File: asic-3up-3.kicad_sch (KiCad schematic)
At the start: 73 parts, among them J10 Conn_01x01, J11 Conn_01x01, J21 Conn_01x01, U4 SN74AVC4T774, U5 25MHz, U66 MCP1824T-1202E/OT, U67 MCP1824T-1202E/OT, U68 MCP1824T-1202E/OT, U69 MCP1824T-0802E, U70 MCP1824T-0802E, U71 MCP1824T-0802E, U72 BM1362AC_MODE1, U73 BM1362AC_MODE0, U74 BM1362AC_MODE1

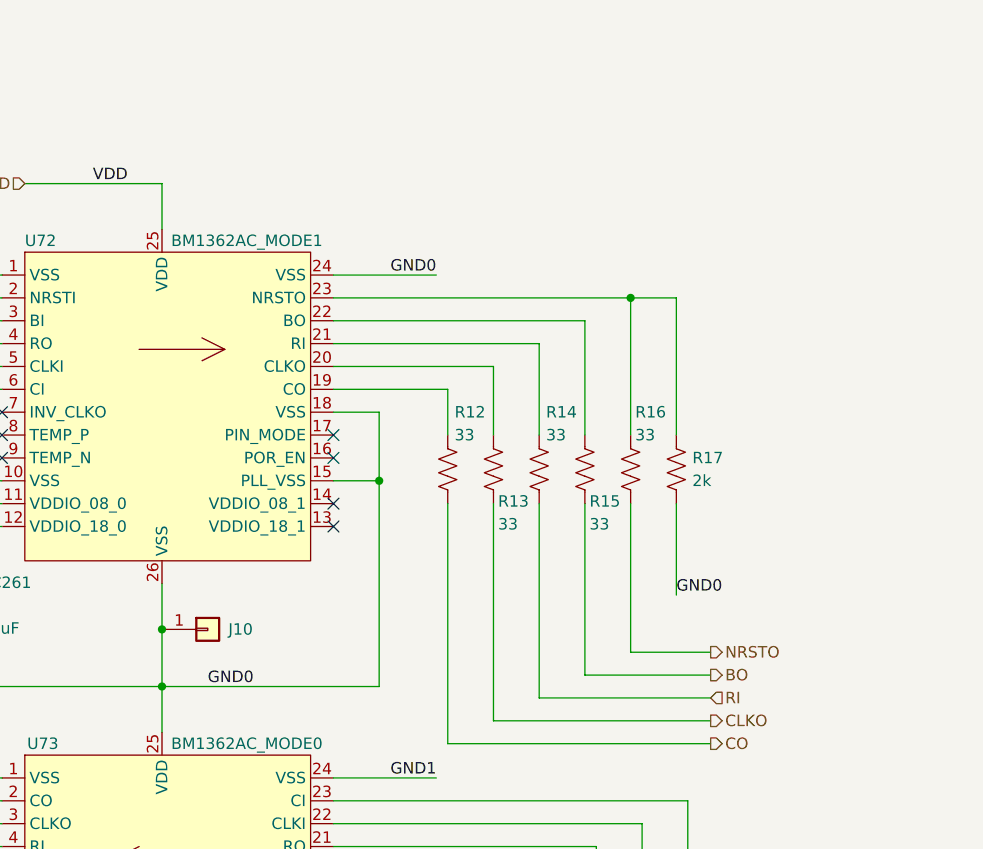
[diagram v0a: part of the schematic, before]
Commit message: added RI pullup resistors for #16. updated BOM. bumped version number to 3
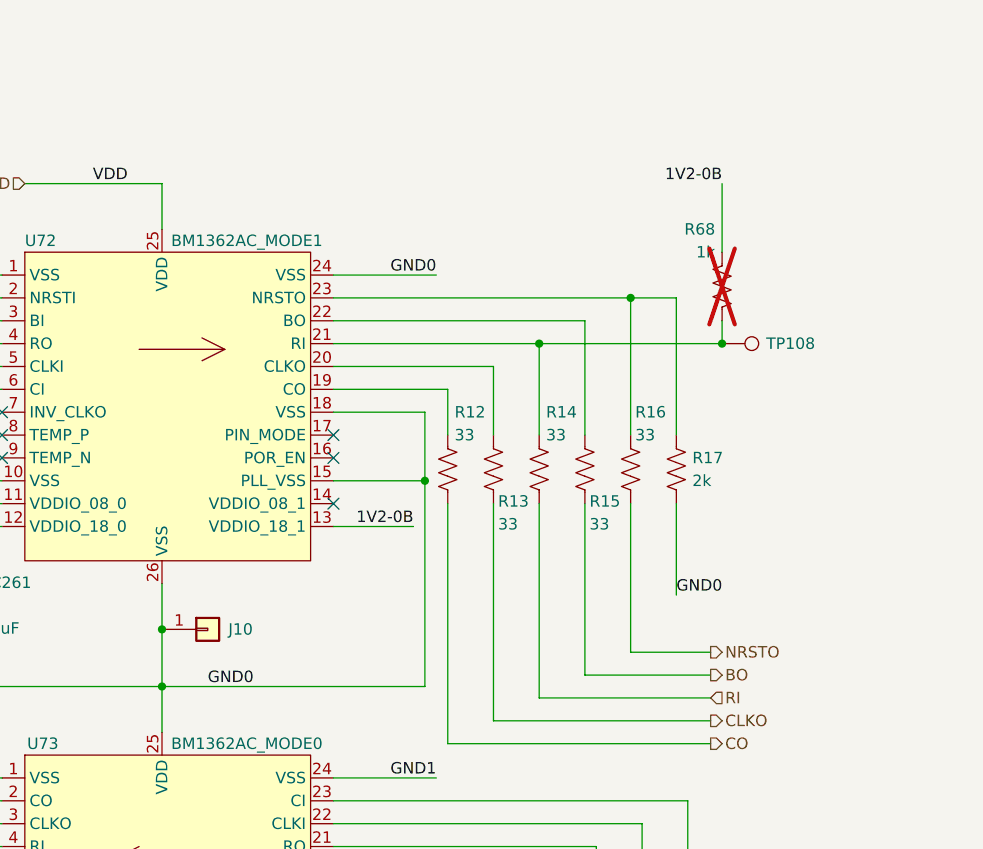
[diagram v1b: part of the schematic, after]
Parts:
- added R68: 1k, Resistor_SMD:R_0402_1005Metric, symbol Device:R_US
- added TP108: TestPoint, TestPoint:TestPoint_Pad_D1.0mm, symbol Connector:TestPoint
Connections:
- net 1V2-0B: now reaches U72.13 (VDDIO_18_1)
- net 1V2-0B: now also R68.1
- net at R14.1, U72.21 (RI): now also R68.2, TP108.1
- no-connect marks 27 -> 26
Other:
- title: (none) -> emberOne/00
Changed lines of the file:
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@@
 	(paper "A3")
 	(title_block
-		(date "2024-11-25")
-		(rev "2")
+		(title "emberOne/00")
+		(date "2025-02-25")
+		(rev "3")
 	)
 	(text "Reference Voltage Regulators"
@@
 	)
 	(junction
+		(at 311.15 105.41)
+		(diameter 0)
+		(color 0 0 0 0)
+	)
+	(junction
 		(at 73.66 64.77)
 		(diameter 0)
@@
 	)
 	(junction
-		(at 273.05 120.65)
-		(diameter 0)
-		(color 0 0 0 0)
-	)
-	(junction
 		(at 220.98 199.39)
 		(diameter 0)
@@
 	)
 	(junction
+		(at 278.13 120.65)
+		(diameter 0)
+		(color 0 0 0 0)
+	)
+	(junction
 		(at 356.87 222.25)
 		(diameter 0)
@@
 	)
 	(junction
+		(at 290.83 105.41)
+		(diameter 0)
+		(color 0 0 0 0)
+	)
+	(junction
 		(at 91.44 163.83)
 		(diameter 0.9144)
@@
 	)
 	(no_connect
-		(at 267.97 125.73)
-	)
-	(no_connect
 		(at 231.14 224.79)
 	)
@@
 	(wire
 		(pts
-			(xy 273.05 113.03) (xy 267.97 113.03)
+			(xy 278.13 113.03) (xy 267.97 113.03)
 		)
 		(stroke
@@
 	(wire
 		(pts
-			(xy 273.05 143.51) (xy 273.05 120.65)
+			(xy 278.13 143.51) (xy 278.13 120.65)
 		)
 		(stroke
@@
 	(wire
 		(pts
-			(xy 248.92 143.51) (xy 273.05 143.51)
+			(xy 248.92 143.51) (xy 278.13 143.51)
 		)
 		(stroke
@@
 	(wire
 		(pts
+			(xy 311.15 87.63) (xy 311.15 95.25)
+		)
+		(stroke
+			(width 0)
+			(type default)
+		)
+	)
+	(wire
+		(pts
 			(xy 207.01 219.71) (xy 207.01 214.63)
 		)
@@
 	(wire
 		(pts
+			(xy 290.83 105.41) (xy 311.15 105.41)
+		)
+		(stroke
+			(width 0)
+			(type default)
+		)
+	)
+	(wire
+		(pts
 			(xy 87.63 166.37) (xy 86.36 166.37)
 		)
@@
 	(wire
 		(pts
-			(xy 267.97 120.65) (xy 273.05 120.65)
+			(xy 267.97 120.65) (xy 278.13 120.65)
 		)
 		(stroke
@@
 	(wire
 		(pts
+			(xy 311.15 105.41) (xy 311.15 102.87)
+		)
+		(stroke
+			(width 0)
+			(type default)
+		)
+	)
+	(wire
+		(pts
 			(xy 152.4 231.14) (xy 152.4 234.95)
 		)
@@
 	(wire
 		(pts
-			(xy 273.05 120.65) (xy 273.05 113.03)
+			(xy 278.13 120.65) (xy 278.13 113.03)
 		)
 		(stroke
@@
 	(wire
 		(pts
+			(xy 267.97 125.73) (xy 276.86 125.73)
+		)
+		(stroke
+			(width 0)
+			(type default)
+		)
+	)
+	(wire
+		(pts
 			(xy 312.42 179.07) (xy 312.42 186.69)
 		)
@@
 		)
 	)
+	(label "1V2-0B"
+		(at 311.15 87.63 180)
+		(effects
+			(font
+				(size 1.27 1.27)
+			)
+			(justify right bottom)
+		)
+	)
 	(label "3V3"
 		(at 106.68 34.29 0)
@@
 		)
 	)
+	(label "1V2-0B"
+		(at 276.86 125.73 180)
+		(effects
+			(font
+				(size 1.27 1.27)
+			)
+			(justify right bottom)
+		)
+	)
 	(label "GND2"
 		(at 105.41 52.07 0)
@@
 	)
 	(symbol
+		(lib_id "Device:R_US")
+		(at 311.15 99.06 0)
+		(mirror y)
+		(unit 1)
+		(exclude_from_sim no)
+		(in_bom yes)
+		(on_board yes)
+		(dnp yes)
+		(property "Reference" "R68"
+			(at 310.388 92.71 0)
+			(effects
+				(font
+					(size 1.27 1.27)
+				)
+				(justify left)
+			)
+		)
+		(property "Value" "1k"
+			(at 310.388 95.25 0)
+			(effects
+				(font
+					(size 1.27 1.27)
+				)
+				(justify left)
+			)
+		)
+		(property "Footprint" "Resistor_SMD:R_0402_1005Metric"
+			(at 310.134 99.314 90)
+			(effects
+				(font
+					(size 1.27 1.27)
+				)
+				(hide yes)
+			)
+		)
+		(property "Datasheet" "~"
+			(at 311.15 99.06 0)
+			(effects
+				(font
+					(size 1.27 1.27)
+				)
+				(hide yes)
+			)
+		)
+		(property "Description" "Resistor, US symbol"
+			(at 311.15 99.06 0)
+			(effects
+				(font
+					(size 1.27 1.27)
+				)
+				(hide yes)
+			)
+		)
+		(property "DK" ""
+			(at 311.15 99.06 0)
+			(effects
+				(font
+					(size 1.27 1.27)
+				)
+				(hide yes)
+			)
+		)
+		(property "PARTNO" ""
+			(at 311.15 99.06 0)
+			(effects
+				(font
+					(size 1.27 1.27)
+				)
+				(hide yes)
+			)
+		)
+		(pin "1"
+		)
+		(pin "2"
+		)
+		(instances
+			(project "emberone"
+				(path "/b036224c-4cdf-48cc-81df-19bc5283ebd2/75fd7cab-4b1e-4fa4-8631-02e52962bbf8"
+					(reference "R68")
+					(unit 1)
+				)
+			)
+		)
+	)
+	(symbol
 		(lib_id "bitaxe:MCP1824")
 		(at 76.2 222.25 0)
@@
 					(unit 1)
 				)
+			)
+		)
+	)
+	(symbol
+		(lib_id "Connector:TestPoint")
+		(at 311.15 105.41 270)
+		(unit 1)
+		(exclude_from_sim no)
+		(in_bom no)
+		(on_board yes)
+		(dnp no)
+		(property "Reference" "TP108"
+			(at 318.77 105.41 90)
+			(effects
+				(font
+					(size 1.27 1.27)
+				)
+			)
+		)
+		(property "Value" "TestPoint"
+			(at 316.865 106.6799 90)
+			(effects
+				(font
+					(size 1.27 1.27)
+				)
+				(justify left)
+				(hide yes)
+			)
+		)
+		(property "Footprint" "TestPoint:TestPoint_Pad_D1.0mm"
+			(at 311.15 110.49 0)
+			(effects
+				(font
+					(size 1.27 1.27)
+				)
+				(hide yes)
+			)
+		)
+		(property "Datasheet" "~"
+			(at 311.15 110.49 0)
+			(effects
+				(font
+					(size 1.27 1.27)
+				)
+				(hide yes)
+			)
+		)
+		(property "Description" ""
+			(at 311.15 105.41 0)
+			(effects
+				(font
+					(size 1.27 1.27)
+				)
+				(hide yes)
+			)
+		)
+		(pin "1"
+		)
+		(instances
+			(project "emberone"
+				(path "/b036224c-4cdf-48cc-81df-19bc5283ebd2/75fd7cab-4b1e-4fa4-8631-02e52962bbf8"
+					(reference "TP108")
+					(unit 1)
+				)

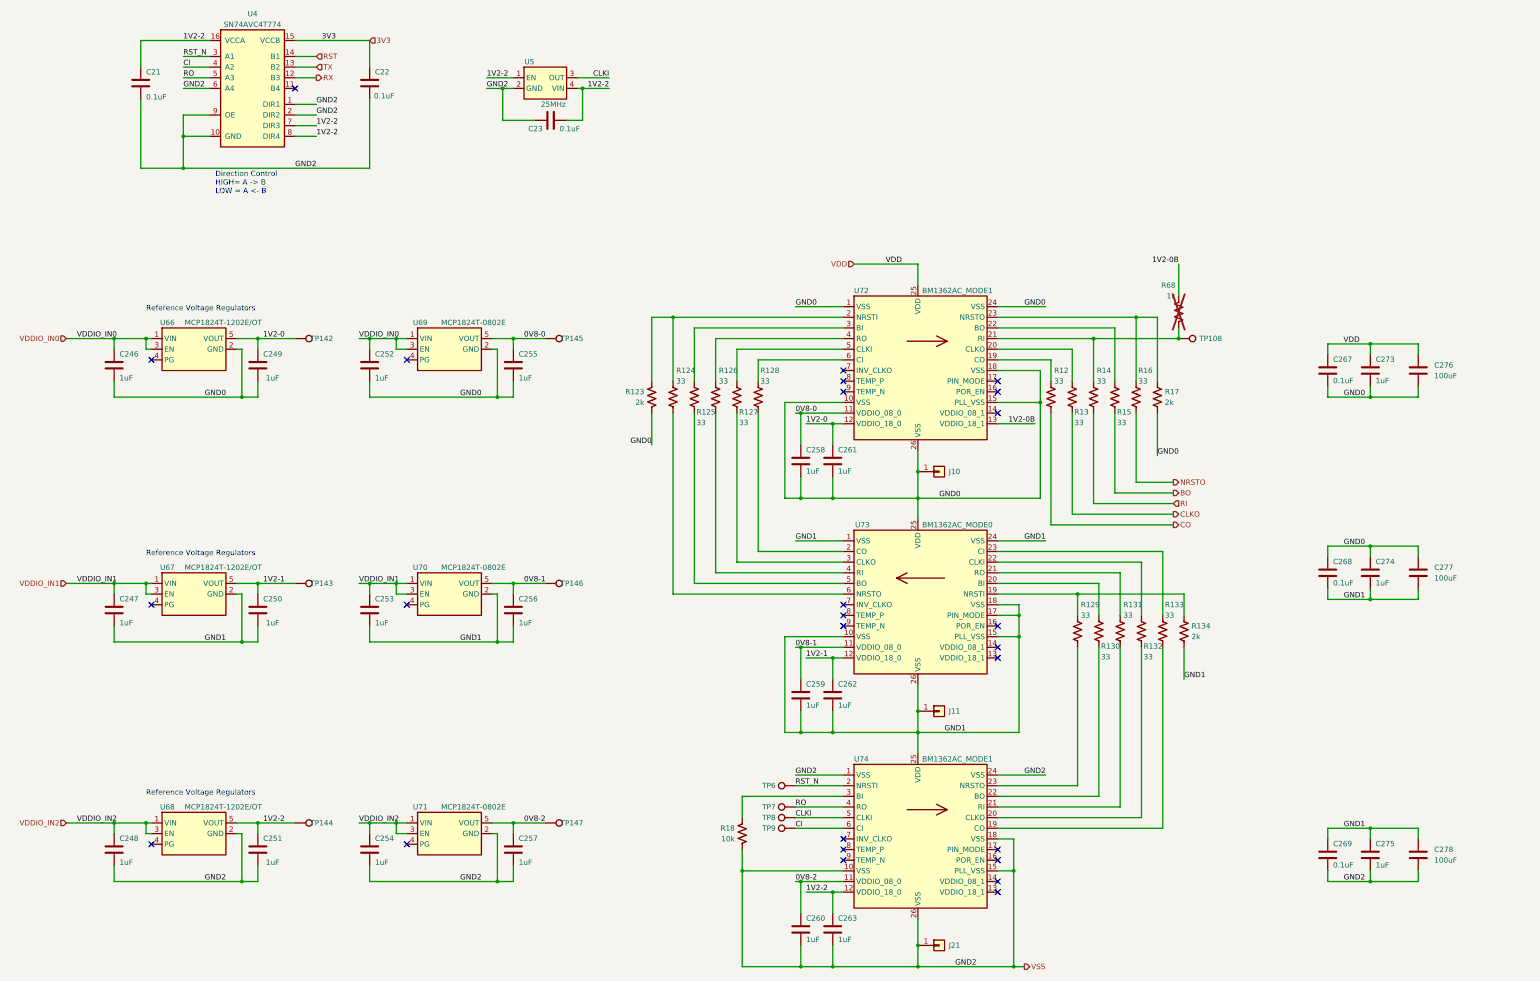
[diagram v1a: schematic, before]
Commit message: added fix for #22. deleted old gerbers
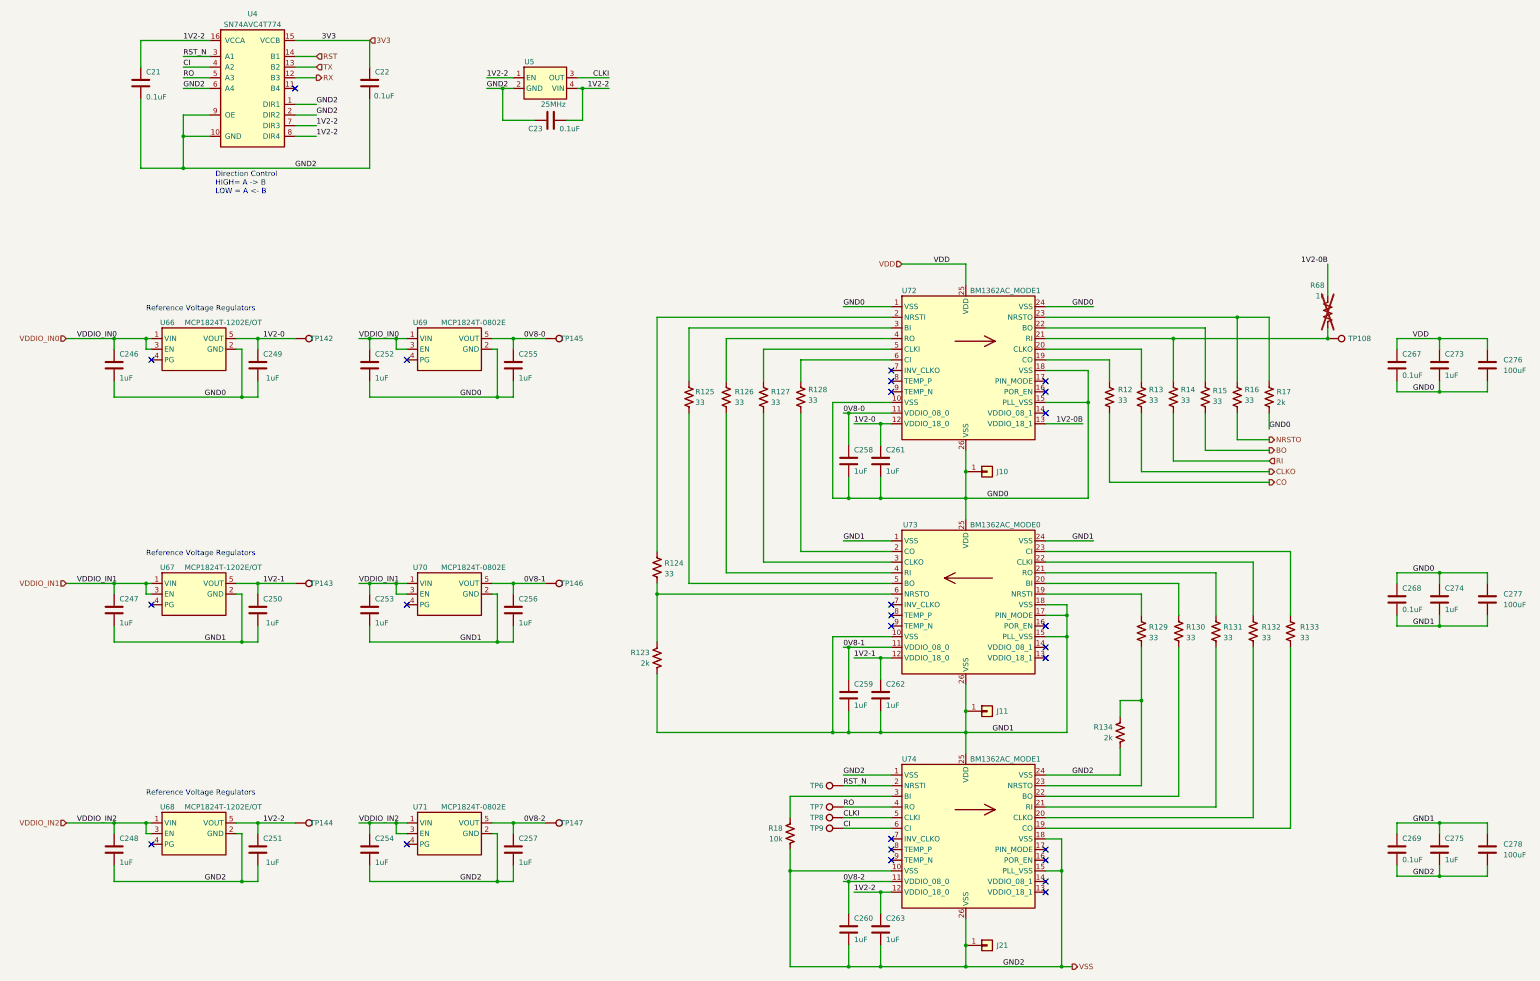
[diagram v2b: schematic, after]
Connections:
- net GND0: no longer R123.2
- net GND1: now also R123.2; no longer R134.2
- net VSS: now also R134.2
- net at R124.1, U72.2 (NRSTI): no longer R123.1
- net at R129.1, U73.19 (NRSTI): no longer R134.1
- net at R124.2, U73.6 (NRSTO): now also R123.1
- net at R129.2, U74.23 (NRSTO): now also R134.1
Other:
- moved on the sheet: C258, C259, C260, C261, C262, C263, C267, C268, C269, C273, C274, C275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

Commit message: added series resistors on data pins between level shifter and 1st ASIC. added pullup on RO
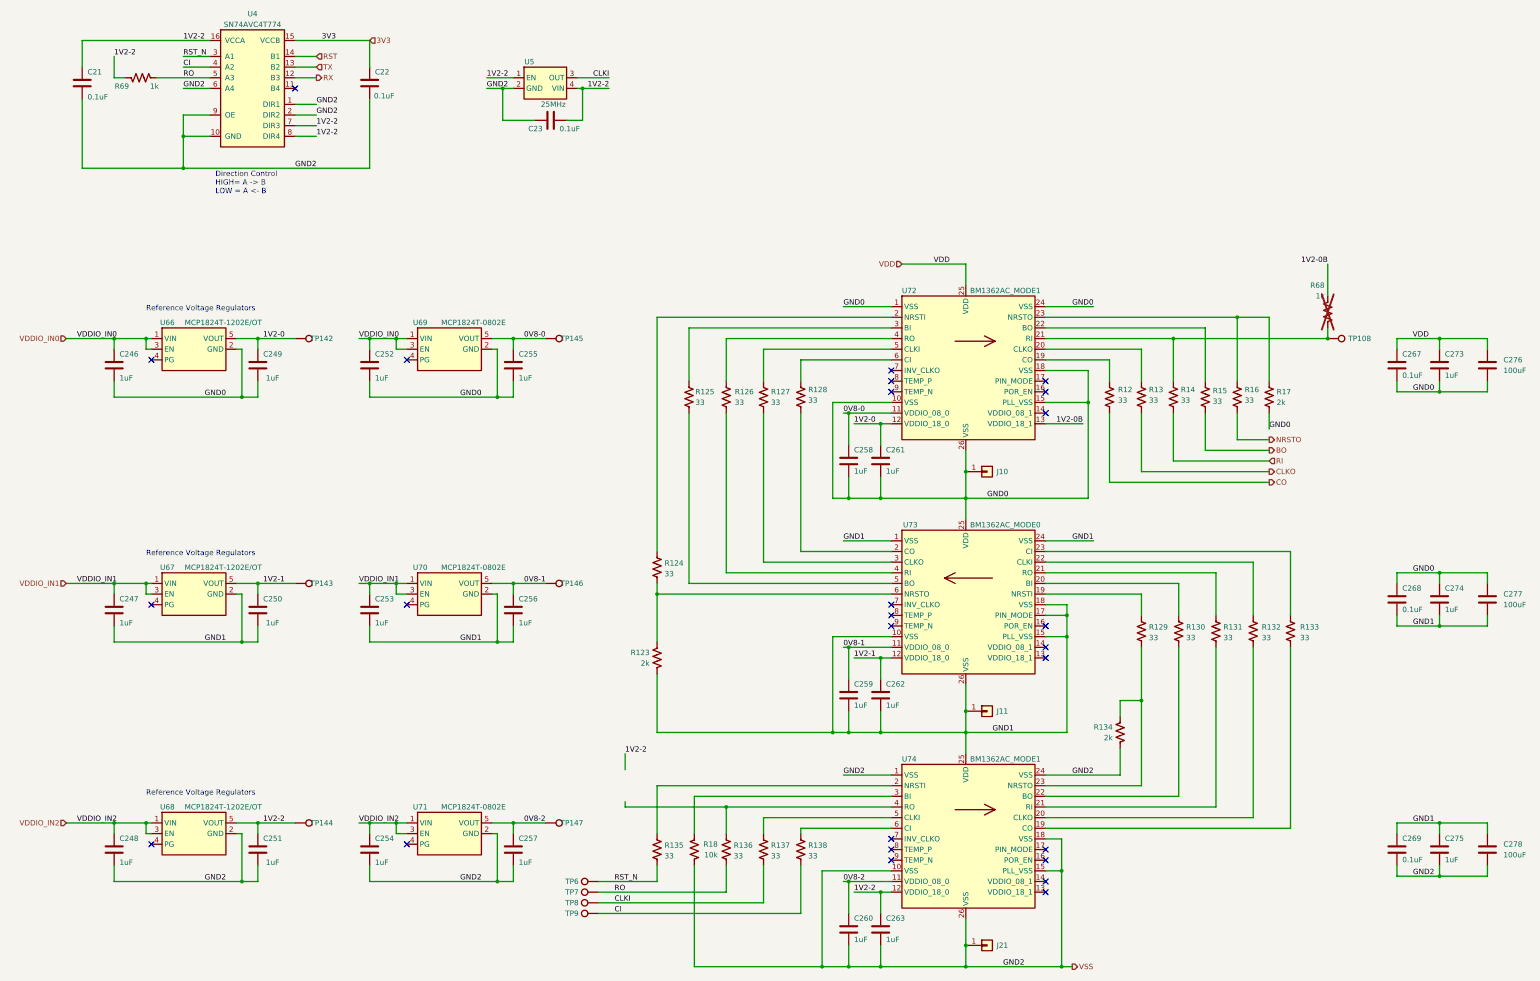
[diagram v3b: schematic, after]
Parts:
- added R135, R136, R137, R138: 33, Resistor_SMD:R_0402_1005Metric, symbol Device:R_US
- added R69: 1k, Resistor_SMD:R_0402_1005Metric, symbol Device:R_US
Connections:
- net 1V2-2: now also R69.1
- net CI: now also R138.2; no longer U74.6 (CI)
- net CLKI: now also R137.2; no longer U74.5 (CLKI)
- net RO: now also R136.2, R69.2; no longer U74.4 (RO)
- net RST_N: now also R135.2; no longer U74.2 (NRSTI)
- new net: R138.1, U74.6 (CI)
- new net: R137.1, U74.5 (CLKI)
- new net: R135.1, U74.2 (NRSTI)
- new net: R136.1, U74.4 (RO)
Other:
- moved on the sheet: C21, R18, TP6, TP7, TP8, TP9

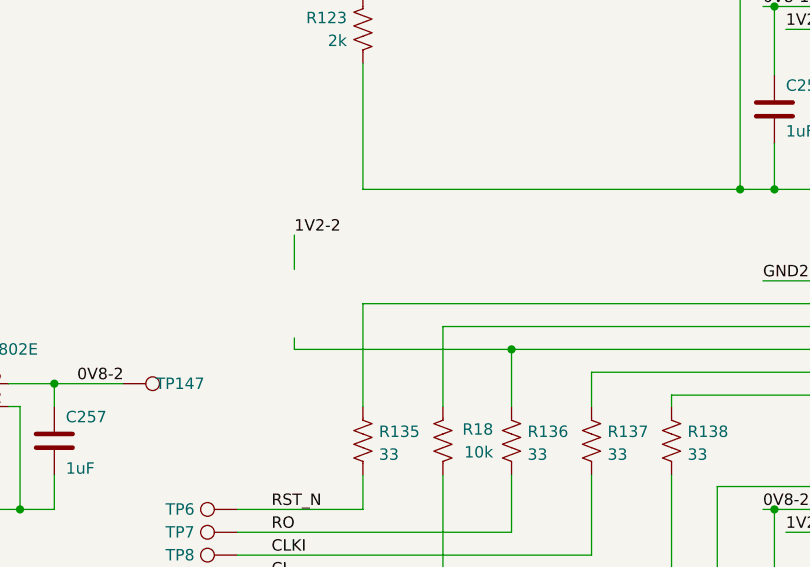
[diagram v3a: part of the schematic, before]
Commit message: reduced center pad paste amount. cleaned up ASIC footprint vias. moved vreg passives around to better fit model name
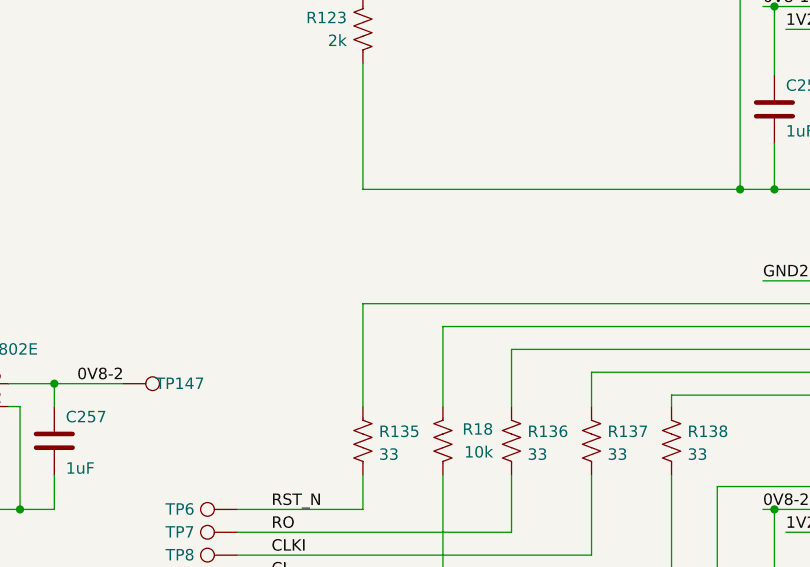
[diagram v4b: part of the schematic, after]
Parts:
- R69: DK (none) -> 311-1.00KLRCT-ND; PARTNO (none) -> RC0402FR-072KL
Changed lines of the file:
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@@
 	)
 	(junction
-		(at 203.2 217.17)
-		(diameter 0)
-		(color 0 0 0 0)
-	)
-	(junction
 		(at 232.41 123.19)
 		(diameter 0)
@@
 	(wire
 		(pts
-			(xy 179.07 204.47) (xy 179.07 208.28)
-		)
-		(stroke
-			(width 0)
-			(type default)
-		)
-	)
-	(wire
-		(pts
 			(xy 242.57 232.41) (xy 226.06 232.41)
 		)
@@
 	(wire
 		(pts
-			(xy 179.07 215.9) (xy 179.07 217.17)
-		)
-		(stroke
-			(width 0)
-			(type default)
-		)
-	)
-	(wire
-		(pts
 			(xy 64.77 107.95) (xy 66.04 107.95)
 		)
@@
 	(wire
 		(pts
-			(xy 179.07 217.17) (xy 203.2 217.17)
-		)
-		(stroke
-			(width 0)
-			(type default)
-		)
-	)
-	(wire
-		(pts
 			(xy 311.15 163.83) (xy 279.4 163.83)
 		)
@@
 		)
 	)
-	(label "1V2-2"
-		(at 179.07 204.47 0)
-		(effects
-			(font
-				(size 1.27 1.27)
-			)
-			(justify left bottom)
-		)
-	)
 	(label "GND0"
 		(at 231.14 97.79 0)
@@
 			)
 		)
-		(property "DK" ""
+		(property "DK" "311-1.00KLRCT-ND"
 			(at 63.5 43.18 0)
 			(effects
@@
 			)
 		)
-		(property "PARTNO" ""
+		(property "PARTNO" "RC0402FR-072KL"
 			(at 63.5 43.18 0)
 			(effects
